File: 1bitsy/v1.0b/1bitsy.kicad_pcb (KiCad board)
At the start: 4 copper layers, 38.1 x 17.8 mm, 94 parts, among them J1 BOOT, P1 CONN_01X01, P10 CONN_01X01, P11 CONN_01X01, P12 CONN_01X01, P13 CONN_01X01, P14 CONN_01X01, P15 CONN_01X01, P16 CONN_01X01, P17 CONN_01X01, P18 CONN_01X01, P19 CONN_01X01, P2 CONN_01X01, P20 CONN_01X01, P21 CONN_01X01, P22 CONN_01X01, P23 CONN_01X01, P24 USB_OTG, P25 CONN_01X01, P26 CONN_01X01, P27 CONN_01X01, P28 CONN_01X01, P29 CONN_01X01, P3 CONN_01X01, P30 CONN_01X01, P31 CONN_01X01, P32 CONN_01X01, P33 CONN_01X01, P34 CONN_01X01, P35 CONN_01X01, P36 CONN_01X01, P37 CONN_01X01, P38 CONN_01X01, P39 CONN_01X01, P4 CONN_01X01, P40 CONN_01X01, P41 CONN_01X01, P42 CONN_01X01, P43 CONN_01X01, P44 CONN_01X01, P45 CONN_01X01, P46 CONN_01X01, P47 CONN_01X01, P48 CONN_01X01, P49 CONN_01X01, P5 CONN_01X01, P50 CONN_01X01, P51 CONN_01X01, P52 CONN_01X01, P6 CONN_01X01, P7 CONN_01X01, P8 CONN_01X01, P9 CONN_01X01, SW1 TACT_G, U1 VREG_3V3, U2 STM32F415RGT, X1 32.768kHz, X2 25MHz, X3 JTAG-10

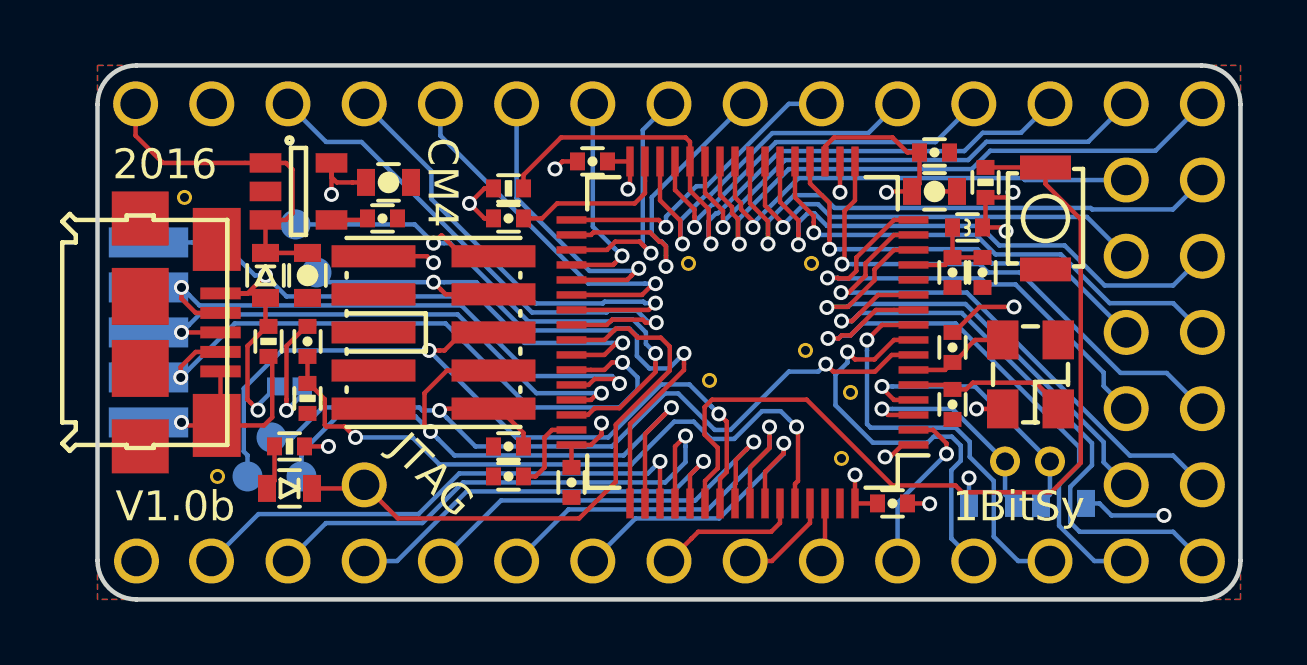
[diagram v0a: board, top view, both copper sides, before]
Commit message: First routing pass on 1BitSy V1.0b.
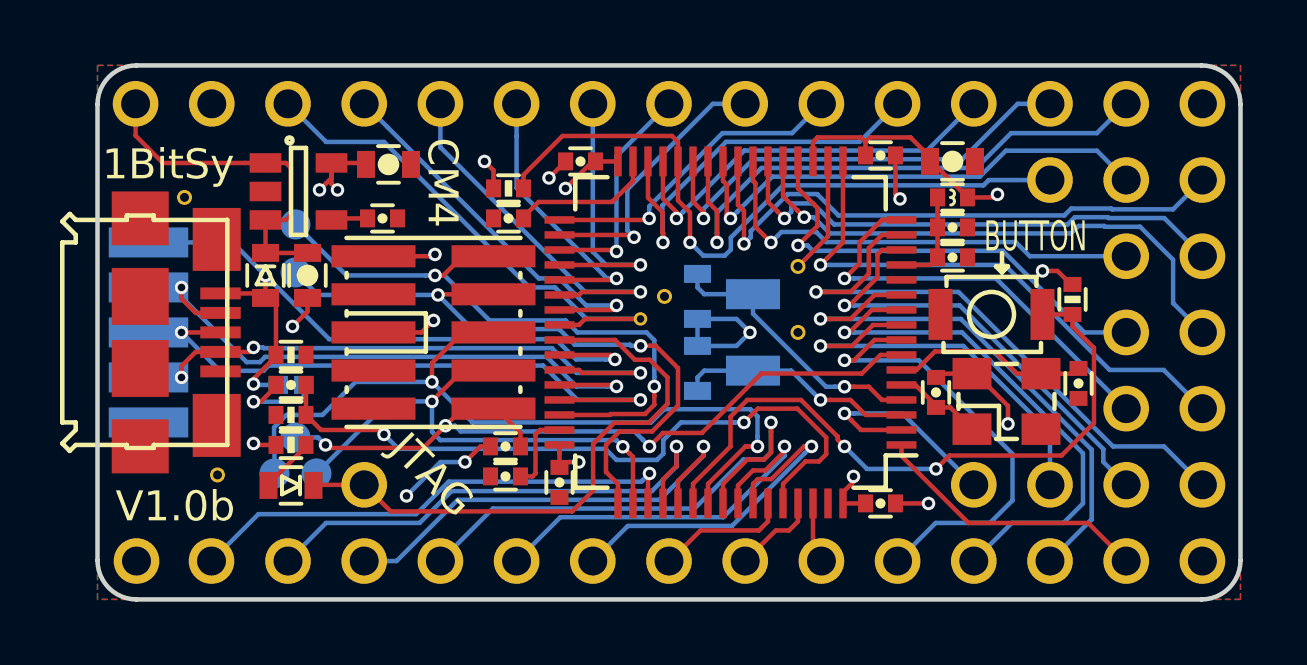
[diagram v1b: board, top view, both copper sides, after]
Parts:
- removed the REF** at (125.1, 49.9)
- removed the REF** at (125.4, 47.7)
- removed the REF** at (120.7, 47.3)
- removed the REF** at (123.9, 46.3)
- removed the REF** at (124.1, 43.4)
- removed the REF** at (120.0, 43.4)
- added P53: CONN_01X01, pkl_pin_headers:Pin_Header_Straight_Round_1x01, F.Cu at (134.6, 53.3)
- added P54: CONN_01X01, pkl_pin_headers:Pin_Header_Straight_Round_1x01, F.Cu at (137.2, 53.3)
- added P55: CONN_01X01, pkl_pin_headers:Pin_Header_Straight_Round_1x01, F.Cu at (137.2, 38.1)
- added REF**: via0305, pkl_misc:via0305, F.Cu at (119.2, 44.5)
- added REF**: via0305, pkl_misc:via0305, F.Cu at (123.7, 45.7)
- added REF**: via0305, pkl_misc:via0305, F.Cu at (123.7, 43.5)
- added REF**: via025045, pkl_misc:via025045, F.Cu at (118.4, 45.3)
- P43, P44, P45, P46, P47: value CONN_01X01 -> TP; footprint pkl_pads:PAD_SMD_R_1x1 -> pkl_pads:POGO_PAD_SMD_R_1x1
- X1: footprint Crystals:Crystal_Round_Horizontal_2mm -> pkl_misc:ABS07
- moved C7 14.0 mm to (120.3, 44.5), turned to 90 degrees
- moved C6 10.8 mm to (120.3, 46.9), turned to 270 degrees
- moved X1 10.1 mm to (122.2, 45.7), turned to 270 degrees
- moved P12 5.08 mm to (129.5, 53.3)
- moved P13 5.08 mm to (132.1, 53.3)
- moved R5 4.86 mm to (132.8, 44.6), turned to 270 degrees
- moved C9 4.37 mm to (133.0, 47.4), turned to 90 degrees
- moved SW1 3.67 mm to (130.1, 45.1)
- moved P23 3.59 mm to (129.5, 50.8)
- moved P11 2.54 mm to (132.1, 50.8)
- moved P27 2.54 mm to (132.1, 40.6)
- moved P10 2.54 mm to (127.0, 53.3)
- moved P25 2.54 mm to (134.6, 38.1)
- moved P26 2.54 mm to (132.1, 38.1)
- moved C2 1.80 mm to (128.8, 42.2), turned to 0 degrees
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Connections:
- U2 pad 1: +3V3 -> /VBAT
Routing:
- net /VBAT: track 0.00 -> 9.31 mm
- net /BUTTON: track 30.2 -> 22.3 mm, vias 0 -> 2
- net /JTAG_TDI: track 22.4 -> 16.9 mm
- net GND: track 19.4 -> 24.4 mm
- net /USB_ID: track 22.2 -> 19.0 mm, vias 2 -> 3
- net /OSC_OUT: track 3.42 -> 6.53 mm
- net /PB4: track 14.4 -> 17.2 mm
- net /PC8: track 16.0 -> 13.2 mm
- net /PC3: track 20.9 -> 18.2 mm
- net /JTAG_RST: track 28.4 -> 25.7 mm, vias 2 -> 3
- net /USB_D+: track 17.7 -> 20.4 mm
- net /OSC_IN: track 5.42 -> 3.00 mm
- net /PB1: track 17.7 -> 15.4 mm
- net /PB15: track 7.28 -> 9.40 mm
- net /USB_VBUS: track 27.7 -> 25.6 mm
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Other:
- net class Default: clearance 0.15 -> 0.14; via_dia 0.5 -> 0.45; via_drill 0.3 -> 0.25
- rule trace_clearance: 0.15 -> 0.14
- rule via_min_drill: 0.3 -> 0.25
- rule via_min_size: 0.5 -> 0.45
- board text added: "BUTTON"
- board text removed: "2016"

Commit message: Some more layout and legend cleanup.
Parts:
- removed the REF** at (118.4, 45.3)
- added REF**: via0305, pkl_misc:via0305, F.Cu at (119.2, 45.4)
- added REF**: via0305, pkl_misc:via0305, F.Cu at (126.1, 49.5)
- added REF**: via0305, pkl_misc:via0305, F.Cu at (110.7, 41.1)
- added REF**: via0305, pkl_misc:via0305, F.Cu at (102.8, 51.0)
- moved REF** 1.50 mm to (122.2, 45.7)
- moved REF** 1.36 mm to (122.3, 43.4)
- moved REF** 1.00 mm to (119.2, 43.5)
- moved LOGO1 0.23 mm to (113.5, 45.7)
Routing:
- net GND: track 24.4 -> 21.8 mm, vias 10 -> 12
- net /PA4: track 15.5 -> 17.1 mm
- net /PA3: track 18.5 -> 19.9 mm
- net +3V3: track 20.9 -> 22.1 mm, vias 9 -> 10
- net /JTAG_TDI: track 16.9 -> 17.6 mm
- net /PA6: track 17.3 -> 16.8 mm
- net /PC9: vias 0 -> 1
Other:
- net class Default: clearance 0.14 -> 0.149
- rule trace_clearance: 0.14 -> 0.149
- board text added: "BOOT DFU"
- board text added: "PA8"
- board text added: "PB2"
- board text added: "PC1"
- board text added: "PC13"
- board text added: "PD2"
- board text added: "RTC 36KHz"
- board text removed: "BOOT"

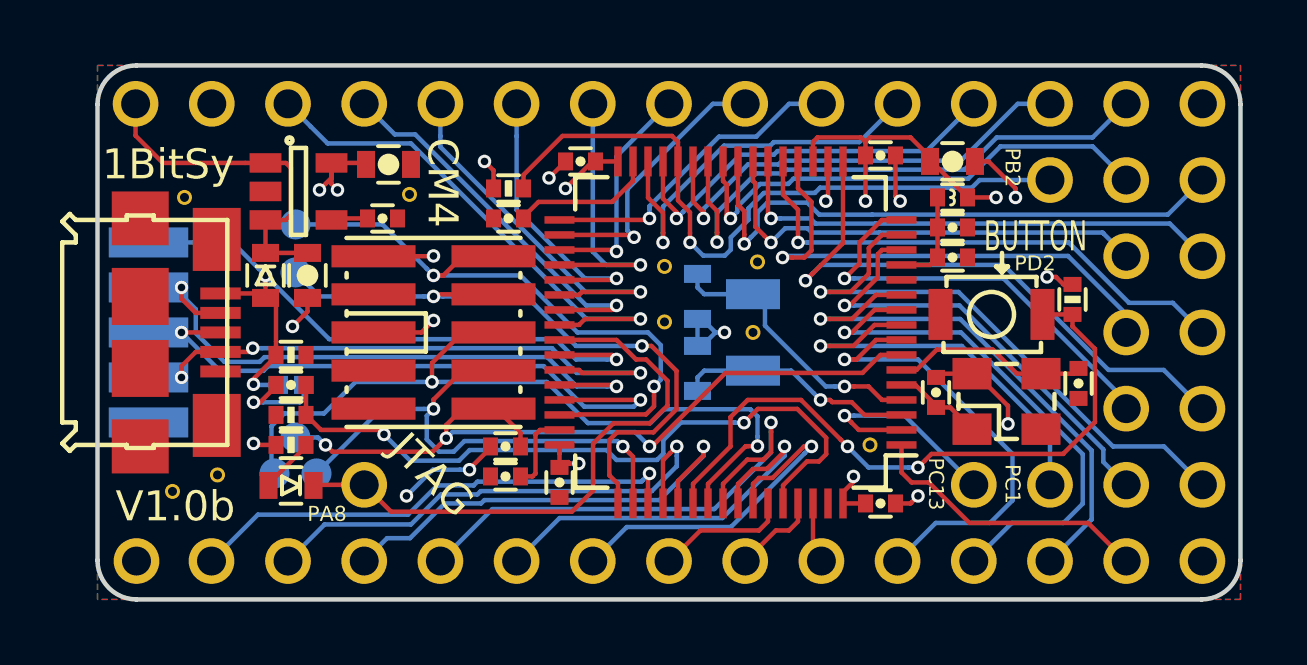
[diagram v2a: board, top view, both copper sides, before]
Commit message: Swapped PA6/PA7 pads to follow pattern. Added pin legend.
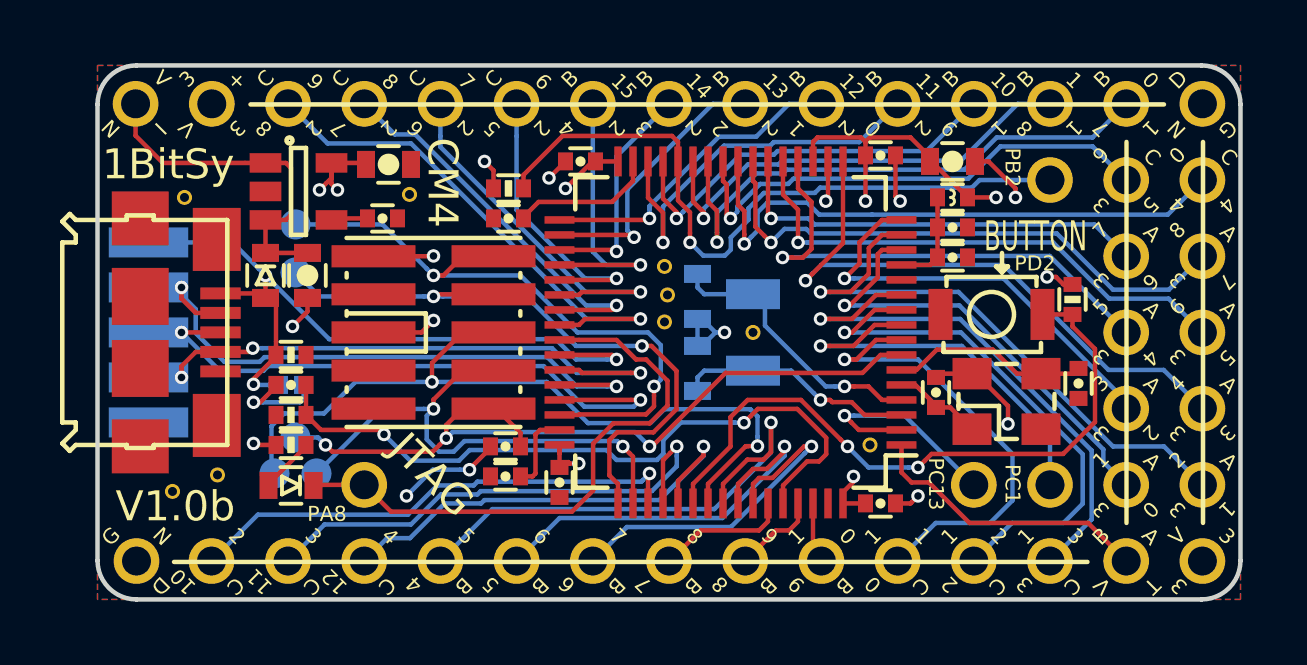
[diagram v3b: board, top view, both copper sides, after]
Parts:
- moved REF** 3.20 mm to (119.3, 44.5)
- moved P7 2.54 mm to (134.6, 43.2)
- moved P8 2.54 mm to (137.2, 43.2)
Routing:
- net /PA7: track 15.4 -> 18.8 mm
- net /PA6: track 16.8 -> 14.3 mm
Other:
- board text added: "+"
- board text added: "0"
- board text added: "A"
- board text added: "B"
- board text added: "C"
- board text added: "D"
- board text added: "G"
- board text added: "I"
- board text added: "N"
- board text added: "T"
- board text added: "V"

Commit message: Some more silkscreen legend cleanup.
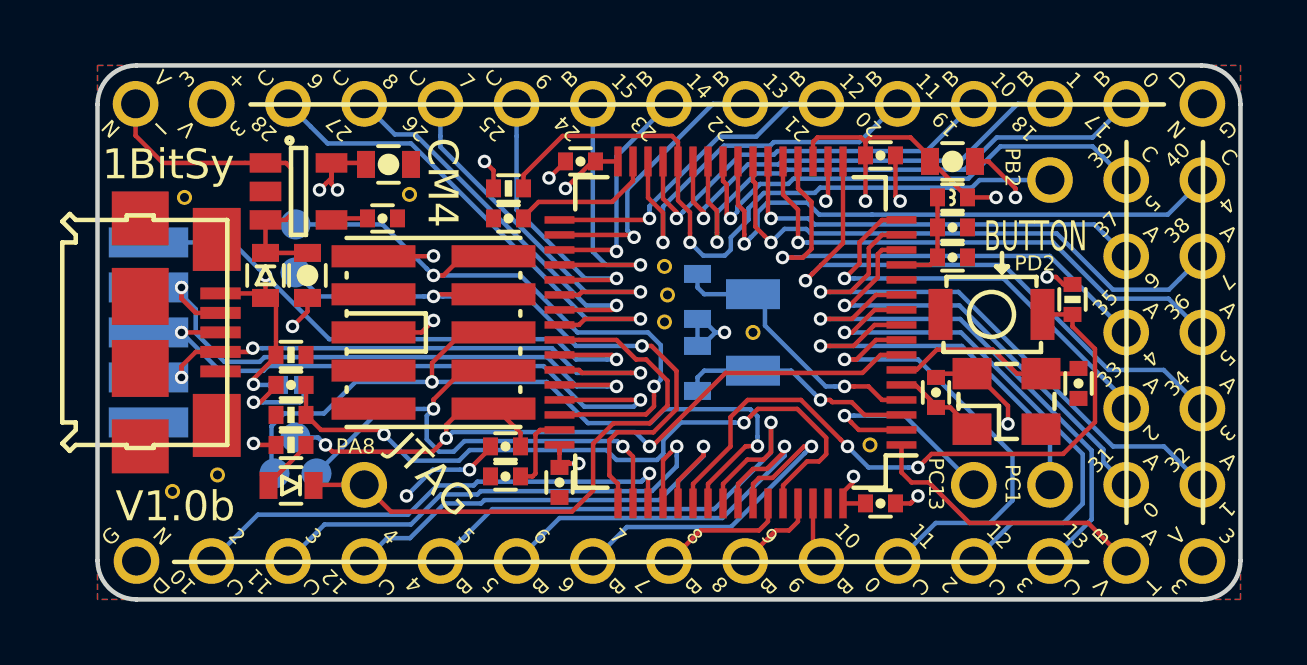
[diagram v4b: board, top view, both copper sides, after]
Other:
- board text added: "31"
- board text added: "32"
- board text added: "33"
- board text added: "34"
- board text added: "35"
- board text added: "36"
- board text added: "37"
- board text added: "38"
- board text added: "39"
- board text added: "40"
